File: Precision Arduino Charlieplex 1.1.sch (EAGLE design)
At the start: 152 parts, among them U401 ATMEGA328, U501 FT232RLSSOP, U602 ZF7, Y401 12.00

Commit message: IMUinator was just a copy of Logomatic. Added a .gitignore file. Updated Precision to have all the LEDs in the right color so that add-digikey.ulp works properly.
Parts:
- added D200, D201, D202, D203, D204, D205, D206, D207, D208, D209, D210, D211, D212, D213, D214, D215, D216, D217, D218, D219, D220, D221, D222, D223, D224, D225, D226, D227, D228, D229, D230, D231, D232, D233, D234, D235, D236, D237, D238, D239, D240, D241, D242, D243, D244, D245, D246, D247, D248, D249, D250, D251, D252, D253, D254, D255, D256, D257, D258, D259: GREEN, SparkFun-LED:LED0603
- added D300, D301, D302, D303, D304, D305, D306, D307, D308, D309, D310, D311, D312, D313, D314, D315, D316, D317, D318, D319, D320, D321, D322, D323, D324, D325, D326, D327, D328, D329, D330, D331, D332, D333, D334, D335, D336, D337, D338, D339, D340, D341, D342, D343, D344, D345, D346, D347, D348, D349, D350, D351, D352, D353, D354, D355, D356, D357, D358, D359: BLUE, SparkFun-LED:LED0603
- C010, C418: DIGIKEY (none) -> 445-7483-1-ND
- C407, C408: DIGIKEY (none) -> 478-6025-1-ND
- C420, C502: DIGIKEY (none) -> 445-1316-1-ND
- D000, D001, D002, D003, D004, D005, D006, D007, D008, D009, D010, D011, D012, D013, D014, D015, D016, D017, D018, D019, D020, D021, D022, D023, D024, D025, D026, D027, D028, D029, D030, D031, D032, D033, D034, D035, D036, D037, D038, D039, D040, D041, D042, D043, D044, D045, D046, D047, D048, D049, D050, D051, D052, D053, D054, D055, D056, D057, D058, D059: value HOUR -> RED; device SparkFun:LED0603 -> SparkFun-LED:LED0603; DIGIKEY (none) -> 754-1359-1-ND
- D100, D101, D102, D103, D104, D105, D106, D107, D108, D109, D110, D111, D112, D113, D114, D115, D116, D117, D118, D119, D120, D121, D122, D123, D124, D125, D126, D127, D128, D129, D130, D131, D132, D133, D134, D135, D136, D137, D138, D139, D140, D141, D142, D143, D144, D145, D146, D147, D148, D149, D150, D151, D152, D153, D154, D155, D156, D157, D158, D159: value HOUR -> YELLOW; device SparkFun:LED0603 -> SparkFun-LED:LED0603; DIGIKEY (none) -> 754-1124-1-ND
- D501: DIGIKEY (none) -> 350-2037-1-ND
- D502: DIGIKEY (none) -> 754-1359-1-ND
- J001, J002, J003, J004, J005, J405, J406, JP1, JP2, JP3, JP4, JP5: DIGIKEY (none) -> $NOPART
- R1, R2, R3, R4: DIGIKEY (none) -> CRA4S847CT-ND
- R501, R502: DIGIKEY (none) -> P680GCT-ND
- R606: DIGIKEY (none) -> CRA4S810KCT-ND
- S429: DIGIKEY (none) -> SW1021CT-ND
- U401: DIGIKEY (none) -> ATMEGA328P-15AZCT-ND
- U501: DIGIKEY (none) -> 768-1007-1-ND
- U602: DIGIKEY (none) -> NC7SZ157P6XCT-ND
- Y401: value 12.00 -> 16MHz; DIGIKEY (none) -> 887-1319-1-ND

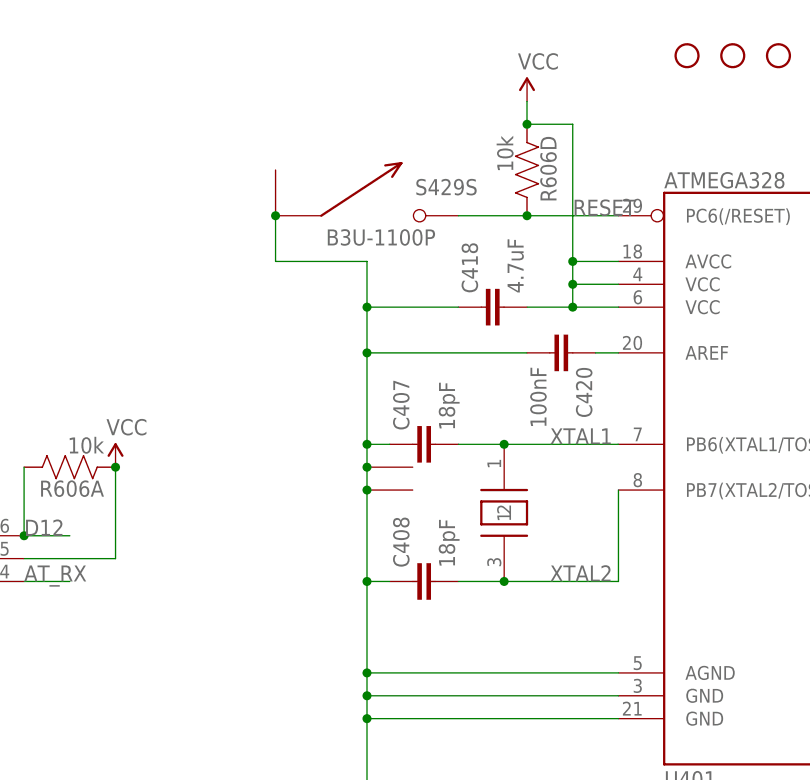
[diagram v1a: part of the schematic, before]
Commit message: Merged Mio's KwanSystems.lbr, updated all eagle files to use it.
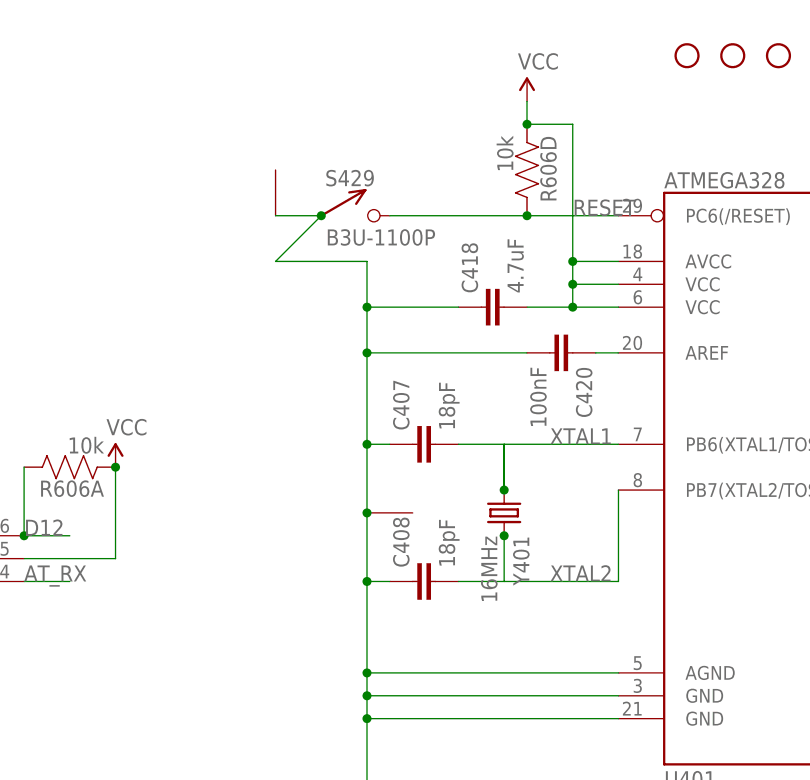
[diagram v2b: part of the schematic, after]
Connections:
- net GND: no longer Y401G$2.1
- net XTAL1: now also Y401_.1; no longer Y401G$3.1
- net XTAL2: now also Y401_.2; no longer Y401G$3.2
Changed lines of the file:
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@@
 </instance>
 <instance part="GND4" gate="1" x="-261.62" y="53.34"/>
-<instance part="Y401" gate="G$1" x="-261.62" y="91.44" rot="R270">
-<attribute name="DIGIKEY" x="-261.62" y="91.44" size="1.778" layer="96" display="off"/>
-</instance>
-<instance part="Y401" gate="G$2" x="-261.62" y="88.9" rot="R270"/>
-<instance part="Y401" gate="G$3" x="-246.38" y="86.36" rot="R270"/>
+<instance part="Y401" gate="G$1" x="-261.62" y="86.36" rot="R270">
+<attribute name="DIGIKEY" x="-261.62" y="86.36" size="1.778" layer="96" display="off"/>
+</instance>
+<instance part="Y401" gate="_" x="-246.38" y="86.36" rot="R270"/>
 <instance part="J001" gate="G$1" x="-215.9" y="172.72" rot="MR180">
 <attribute name="DIGIKEY" x="-215.9" y="172.72" size="1.778" layer="96" display="off"/>
@@
 <wire x1="-259.08" y1="78.74" x2="-261.62" y2="78.74" width="0.1524" layer="91"/>
 <wire x1="-261.62" y1="78.74" x2="-261.62" y2="68.58" width="0.1524" layer="91"/>
-<wire x1="-261.62" y1="88.9" x2="-261.62" y2="78.74" width="0.1524" layer="91"/>
-<wire x1="-261.62" y1="91.44" x2="-261.62" y2="88.9" width="0.1524" layer="91"/>
+<wire x1="-261.62" y1="86.36" x2="-261.62" y2="78.74" width="0.1524" layer="91"/>
 <wire x1="-259.08" y1="93.98" x2="-261.62" y2="93.98" width="0.1524" layer="91"/>
-<wire x1="-261.62" y1="93.98" x2="-261.62" y2="91.44" width="0.1524" layer="91"/>
+<wire x1="-261.62" y1="93.98" x2="-261.62" y2="86.36" width="0.1524" layer="91"/>
 <wire x1="-261.62" y1="104.14" x2="-261.62" y2="93.98" width="0.1524" layer="91"/>
 <wire x1="-271.78" y1="114.3" x2="-261.62" y2="114.3" width="0.1524" layer="91"/>
@@
 <wire x1="-261.62" y1="109.22" x2="-261.62" y2="104.14" width="0.1524" layer="91"/>
 <wire x1="-243.84" y1="104.14" x2="-261.62" y2="104.14" width="0.1524" layer="91"/>
-<wire x1="-271.78" y1="114.3" x2="-271.78" y2="119.38" width="0.1524" layer="91"/>
+<wire x1="-271.78" y1="114.3" x2="-266.7" y2="119.38" width="0.1524" layer="91"/>
 <junction x="-261.62" y="63.5"/>
 <junction x="-261.62" y="66.04"/>
 <junction x="-261.62" y="68.58"/>
 <junction x="-261.62" y="78.74"/>
-<junction x="-261.62" y="88.9"/>
-<junction x="-261.62" y="91.44"/>
+<junction x="-261.62" y="86.36"/>
 <junction x="-261.62" y="93.98"/>
 <junction x="-261.62" y="109.22"/>
 <junction x="-261.62" y="104.14"/>
-<junction x="-271.78" y="119.38"/>
+<junction x="-266.7" y="119.38"/>
 <pinref part="GND4" gate="1" pin="GND"/>
 <pinref part="U401" gate="G$1" pin="GND@2"/>
@@
 <pinref part="U401" gate="G$1" pin="AGND"/>
 <pinref part="C408" gate="G$1" pin="1"/>
-<pinref part="Y401" gate="G$2" pin="1"/>
 <pinref part="Y401" gate="G$1" pin="1"/>
 <pinref part="C407" gate="G$1" pin="1"/>
@@
 <pinref part="S429" gate="G" pin="1"/>
 <pinref part="S429" gate="S" pin="1"/>
+<wire x1="-271.78" y1="119.38" x2="-266.7" y2="119.38" width="0.1524" layer="91"/>
 </segment>
 <segment>
@@
 <segment>
 <wire x1="-251.46" y1="93.98" x2="-246.38" y2="93.98" width="0.1524" layer="91"/>
+<wire x1="-246.38" y1="93.98" x2="-246.38" y2="88.9" width="0.1524" layer="91"/>
+<wire x1="-246.38" y1="88.9" x2="-246.38" y2="93.98" width="0.1524" layer="91"/>
 <wire x1="-246.38" y1="93.98" x2="-233.68" y2="93.98" width="0.1524" layer="91"/>
-<junction x="-246.38" y="93.98"/>
+<junction x="-246.38" y="88.9"/>
 <label x="-241.3" y="93.98" size="1.778" layer="95"/>
 <pinref part="C407" gate="G$1" pin="2"/>
-<pinref part="Y401" gate="G$3" pin="1"/>
+<pinref part="Y401" gate="_" pin="1"/>
 <pinref part="U401" gate="G$1" pin="PB6(XTAL1/TOSC1)"/>
 </segment>
@@
 <segment>
 <wire x1="-233.68" y1="78.74" x2="-246.38" y2="78.74" width="0.1524" layer="91"/>
+<wire x1="-246.38" y1="83.82" x2="-246.38" y2="78.74" width="0.1524" layer="91"/>
 <wire x1="-246.38" y1="78.74" x2="-251.46" y2="78.74" width="0.1524" layer="91"/>
 <wire x1="-233.68" y1="78.74" x2="-233.68" y2="88.9" width="0.1524" layer="91"/>
-<junction x="-246.38" y="78.74"/>
+<junction x="-246.38" y="83.82"/>
 <label x="-241.3" y="78.74" size="1.778" layer="95"/>
 <pinref part="C408" gate="G$1" pin="2"/>
-<pinref part="Y401" gate="G$3" pin="2"/>
+<pinref part="Y401" gate="_" pin="2"/>
 <pinref part="U401" gate="G$1" pin="PB7(XTAL2/TOSC2)"/>
 </segment>
@@
 <segment>
 <wire x1="-233.68" y1="119.38" x2="-243.84" y2="119.38" width="0.1524" layer="91"/>
-<wire x1="-251.46" y1="119.38" x2="-243.84" y2="119.38" width="0.1524" layer="91"/>
+<wire x1="-259.08" y1="119.38" x2="-243.84" y2="119.38" width="0.1524" layer="91"/>
 <junction x="-243.84" y="119.38"/>
 <label x="-238.76" y="119.38" size="1.778" layer="95"/>
